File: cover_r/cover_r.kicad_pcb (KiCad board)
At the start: 2 copper layers, 24 x 58.2 mm, 2 parts

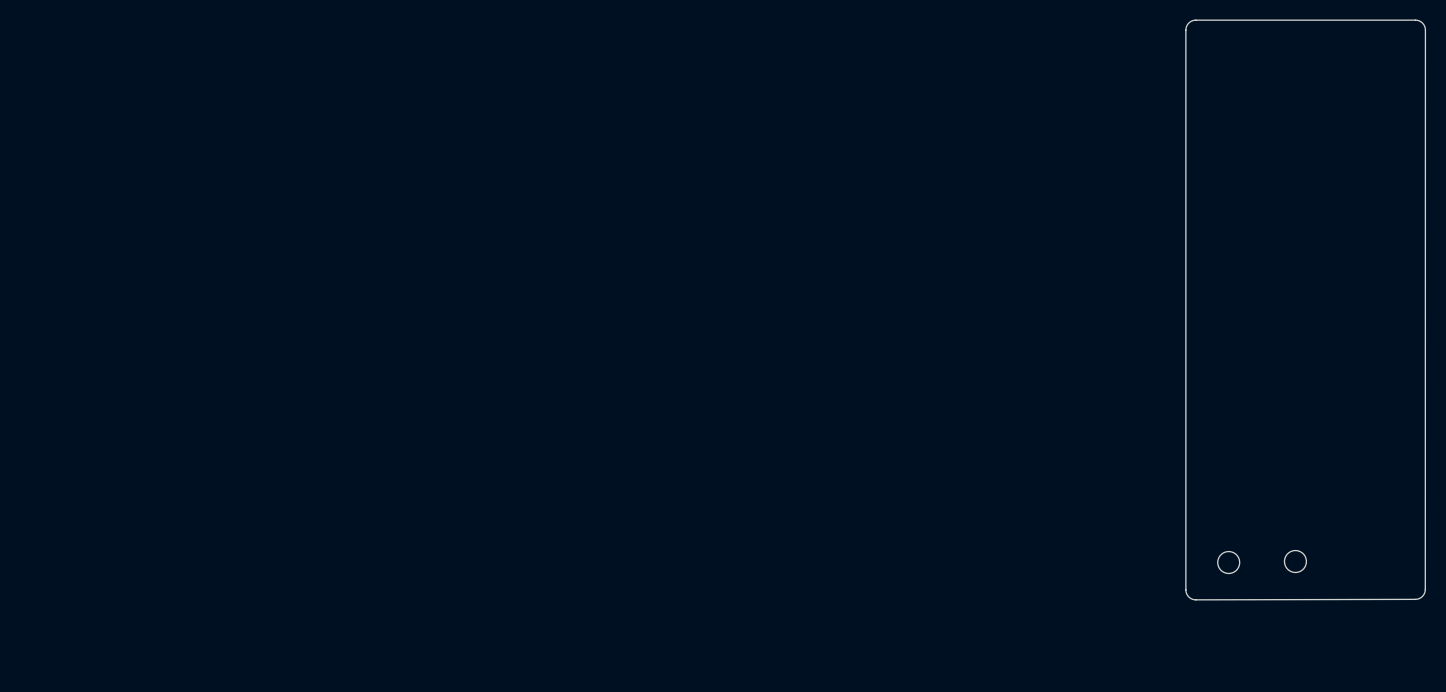
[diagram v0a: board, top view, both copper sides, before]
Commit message: feat: add right cover plate
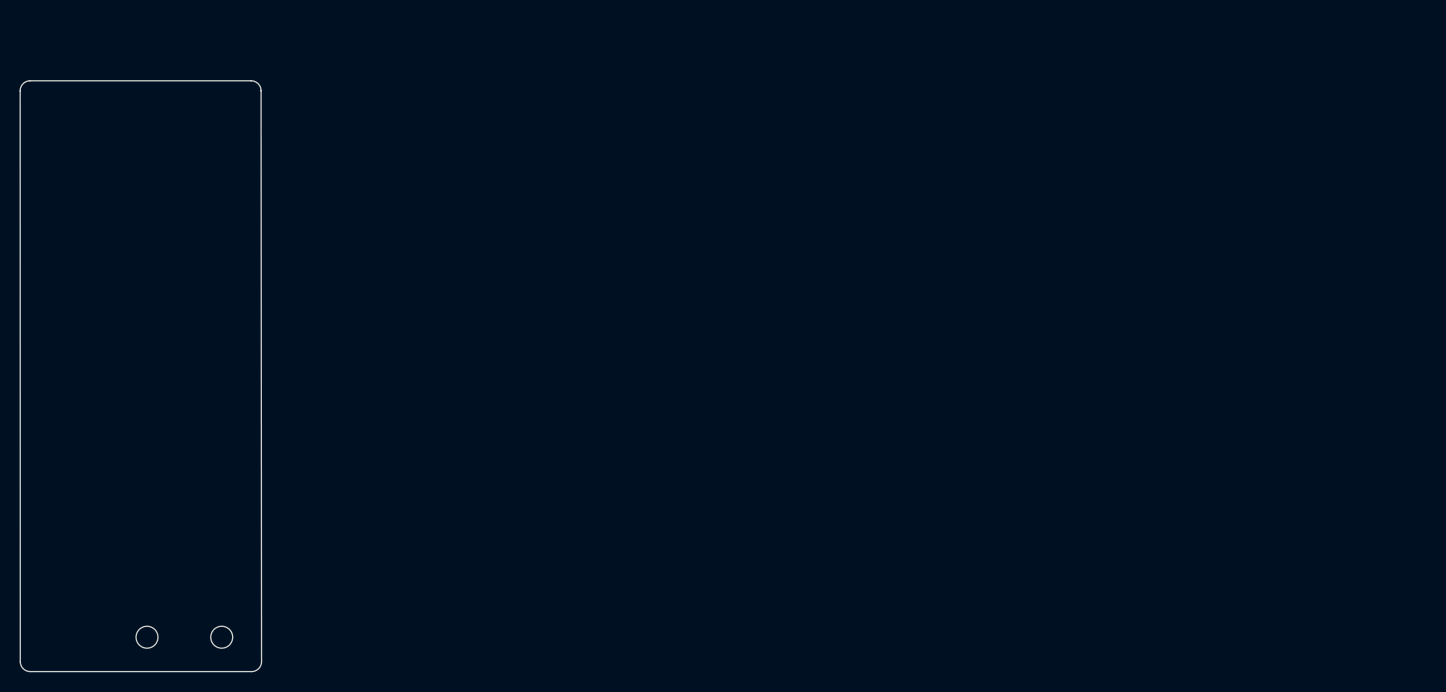
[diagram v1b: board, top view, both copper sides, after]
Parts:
- removed the Ref** at (172.0, 109.4)
- removed the Ref** at (165.3, 109.5)
- added Ref**: Val**, kbd_Hole:m2_Screw_Hole_EdgeCuts, F.Cu at (64.2, 117.0)
- added Ref**: Val**, kbd_Hole:m2_Screw_Hole_EdgeCuts, F.Cu at (56.7, 117.0)
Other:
- board size 24 x 58.2 mm -> 24.2 x 59.3 mm
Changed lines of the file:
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@@
 			(drillshape 0)
 			(scaleselection 1)
-			(outputdirectory "../order_20250402_jcl/assemble_l")
+			(outputdirectory "../order_20250402_jcl/assemble_r")
 		)
 	)
@@
 	(footprint "kbd_Hole:m2_Screw_Hole_EdgeCuts"
 		(layer "F.Cu")
-		(at 172 109.4 -90)
+		(at 64.2 117)
 		(descr "Mounting Hole 2.2mm, no annular, M2")
 		(tags "mounting hole 2.2mm no annular m2")
 		(property "Reference" "Ref**"
-			(at 0 -3.2 270)
+			(at 0 -3.2 0)
 			(layer "F.Fab")
 			(hide yes)
@@
 		)
 		(property "Value" "Val**"
-			(at 0 3.2 270)
+			(at 0 3.2 0)
 			(layer "F.Fab")
 			(hide yes)
@@
 		)
 		(property "Datasheet" ""
-			(at 0 0 270)
+			(at 0 0 0)
 			(layer "F.Fab")
 			(hide yes)
@@
 		)
 		(property "Description" ""
-			(at 0 0 270)
+			(at 0 0 0)
 			(layer "F.Fab")
 			(hide yes)
@@
 		)
 		(fp_text user "${REFERENCE}"
-			(at 0.3 0 270)
+			(at 0.3 0 0)
 			(layer "F.Fab")
 			(hide yes)
@@
 	(footprint "kbd_Hole:m2_Screw_Hole_EdgeCuts"
 		(layer "F.Cu")
-		(at 165.3 109.5 -90)
+		(at 56.7 117)
 		(descr "Mounting Hole 2.2mm, no annular, M2")
 		(tags "mounting hole 2.2mm no annular m2")
 		(property "Reference" "Ref**"
-			(at 0 -3.2 270)
+			(at 0 -3.2 0)
 			(layer "F.Fab")
 			(hide yes)
@@
 		)
 		(property "Value" "Val**"
-			(at 0 3.2 270)
+			(at 0 3.2 0)
 			(layer "F.Fab")
 			(hide yes)
@@
 		)
 		(property "Datasheet" ""
-			(at 0 0 270)
+			(at 0 0 0)
 			(layer "F.Fab")
 			(hide yes)
@@
 		)
 		(property "Description" ""
-			(at 0 0 270)
+			(at 0 0 0)
 			(layer "F.Fab")
 			(hide yes)
@@
 		)
 		(fp_text user "${REFERENCE}"
-			(at 0.3 0 270)
+			(at 0.3 0 0)
 			(layer "F.Fab")
 			(hide yes)
@@
 	)
 	(gr_arc
-		(start 162.002175 113.24782)
-		(mid 161.293663 112.955698)
-		(end 161 112.247823)
-		(stroke
-			(width 0.05)
-			(type default)
-		)
-		(layer "Edge.Cuts")
-	)
-	(gr_arc
-		(start 185.038158 112.200094)
-		(mid 184.745962 112.906291)
-		(end 184.040333 113.199885)
-		(stroke
-			(width 0.05)
-			(type default)
-		)
-		(layer "Edge.Cuts")
-	)
-	(gr_line
-		(start 162 55.05)
-		(end 184.049793 55.05)
-		(stroke
-			(width 0.05)
-			(type default)
-		)
-		(layer "Edge.Cuts")
-	)
-	(gr_arc
-		(start 161 56.05)
-		(mid 161.292893 55.342893)
-		(end 162 55.05)
-		(stroke
-			(width 0.05)
-			(type default)
-		)
-		(layer "Edge.Cuts")
-	)
-	(gr_arc
-		(start 184.049793 55.05)
-		(mid 184.756977 55.342964)
-		(end 185.049793 56.050207)
-		(stroke
-			(width 0.05)
-			(type default)
-		)
-		(layer "Edge.Cuts")
-	)
-	(gr_line
-		(start 161 56.05)
-		(end 161 112.247823)
-		(stroke
-			(width 0.05)
-			(type default)
-		)
-		(layer "Edge.Cuts")
-	)
-	(gr_line
-		(start 162.002175 113.24782)
-		(end 184.040333 113.199885)
-		(stroke
-			(width 0.05)
-			(type default)
-		)
-		(layer "Edge.Cuts")
-	)
-	(gr_line
-		(start 185.049793 56.050207)
-		(end 185.038158 112.200094)
-		(stroke
-			(width 0.05)
+		(start 43.965858 62.137707)
+		(mid 44.258682 61.430487)
+		(end 44.965858 61.1375)
+		(stroke
+			(width 0.05)
+			(type default)
+		)
+		(layer "Edge.Cuts")
+	)
+	(gr_line
+		(start 68.199156 119.449157)
+		(end 68.150842 62.136657)
+		(stroke
+			(width 0.05)
+			(type default)
+		)
+		(layer "Edge.Cuts")
+	)
+	(gr_arc
+		(start 67.150843 61.1375)
+		(mid 67.857624 61.43011)
+		(end 68.150842 62.136657)
+		(stroke
+			(width 0.05)
+			(type default)
+		)
+		(layer "Edge.Cuts")
+	)
+	(gr_line
+		(start 67.199157 120.45)
+		(end 44.977734 120.450005)
+		(stroke
+			(width 0.05)
+			(type default)
+		)
+		(layer "Edge.Cuts")
+	)
+	(gr_arc
+		(start 68.199156 119.449157)
+		(mid 67.906559 120.156793)
+		(end 67.199157 120.45)
+		(stroke
+			(width 0.05)
+			(type default)
+		)
+		(layer "Edge.Cuts")
+	)
+	(gr_arc
+		(start 44.977734 120.450005)
+		(mid 44.2707 120.157185)
+		(end 43.977734 119.450212)
+		(stroke
+			(width 0.05)
+			(type default)
+		)
+		(layer "Edge.Cuts")
+	)
+	(gr_line
+		(start 43.965858 62.137707)
+		(end 43.977734 119.450212)
+		(stroke
+			(width 0.05)
+			(type default)
+		)
+		(layer "Edge.Cuts")
+	)
+	(gr_line
+		(start 67.150843 61.1375)
+		(end 44.965858 61.1375)
+		(stroke
+			(width 0.05)
